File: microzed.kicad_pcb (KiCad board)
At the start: 10 copper layers, 60 x 100 mm, 333 parts, among them IC1 XC7Z020-1CLG484C, IC2 RTL8211E-VL-CG, J1 640456-3, J2 10104111-0001LF, J3 L829-1J1T-43, J4 Micro_SD_Card_Det_Hirose_DM3AT, J5 10104111-0001LF, J6 BSH-090-01-X-D-A, J7 BSH-090-01-X-D-A, Q1 MMBT3904, Q2 MMBT3904, SW1 SW_Push, U1 TLV62130RGTR, U10 MT41K256M16TW, U11 MT25QL128ABA8E12-1SIT, U12 USB3320C-EZK, U13 ASDMB-24.000MHZ-LC-T, U14 ASDMB-25.000MHZ-LC-T, U15 TXS02612RTWR, U16 CP2104-F03-GM, U2 TLV62130RGTR, U3 TLV62130RGTR, U4 TLV62130RGTR, U5 TLV62130RGTR, U6 ASDMB-33.333MHZ-LC-T, U7 TPS51206DSQR, U8 REF3012, U9 MT41K256M16TW

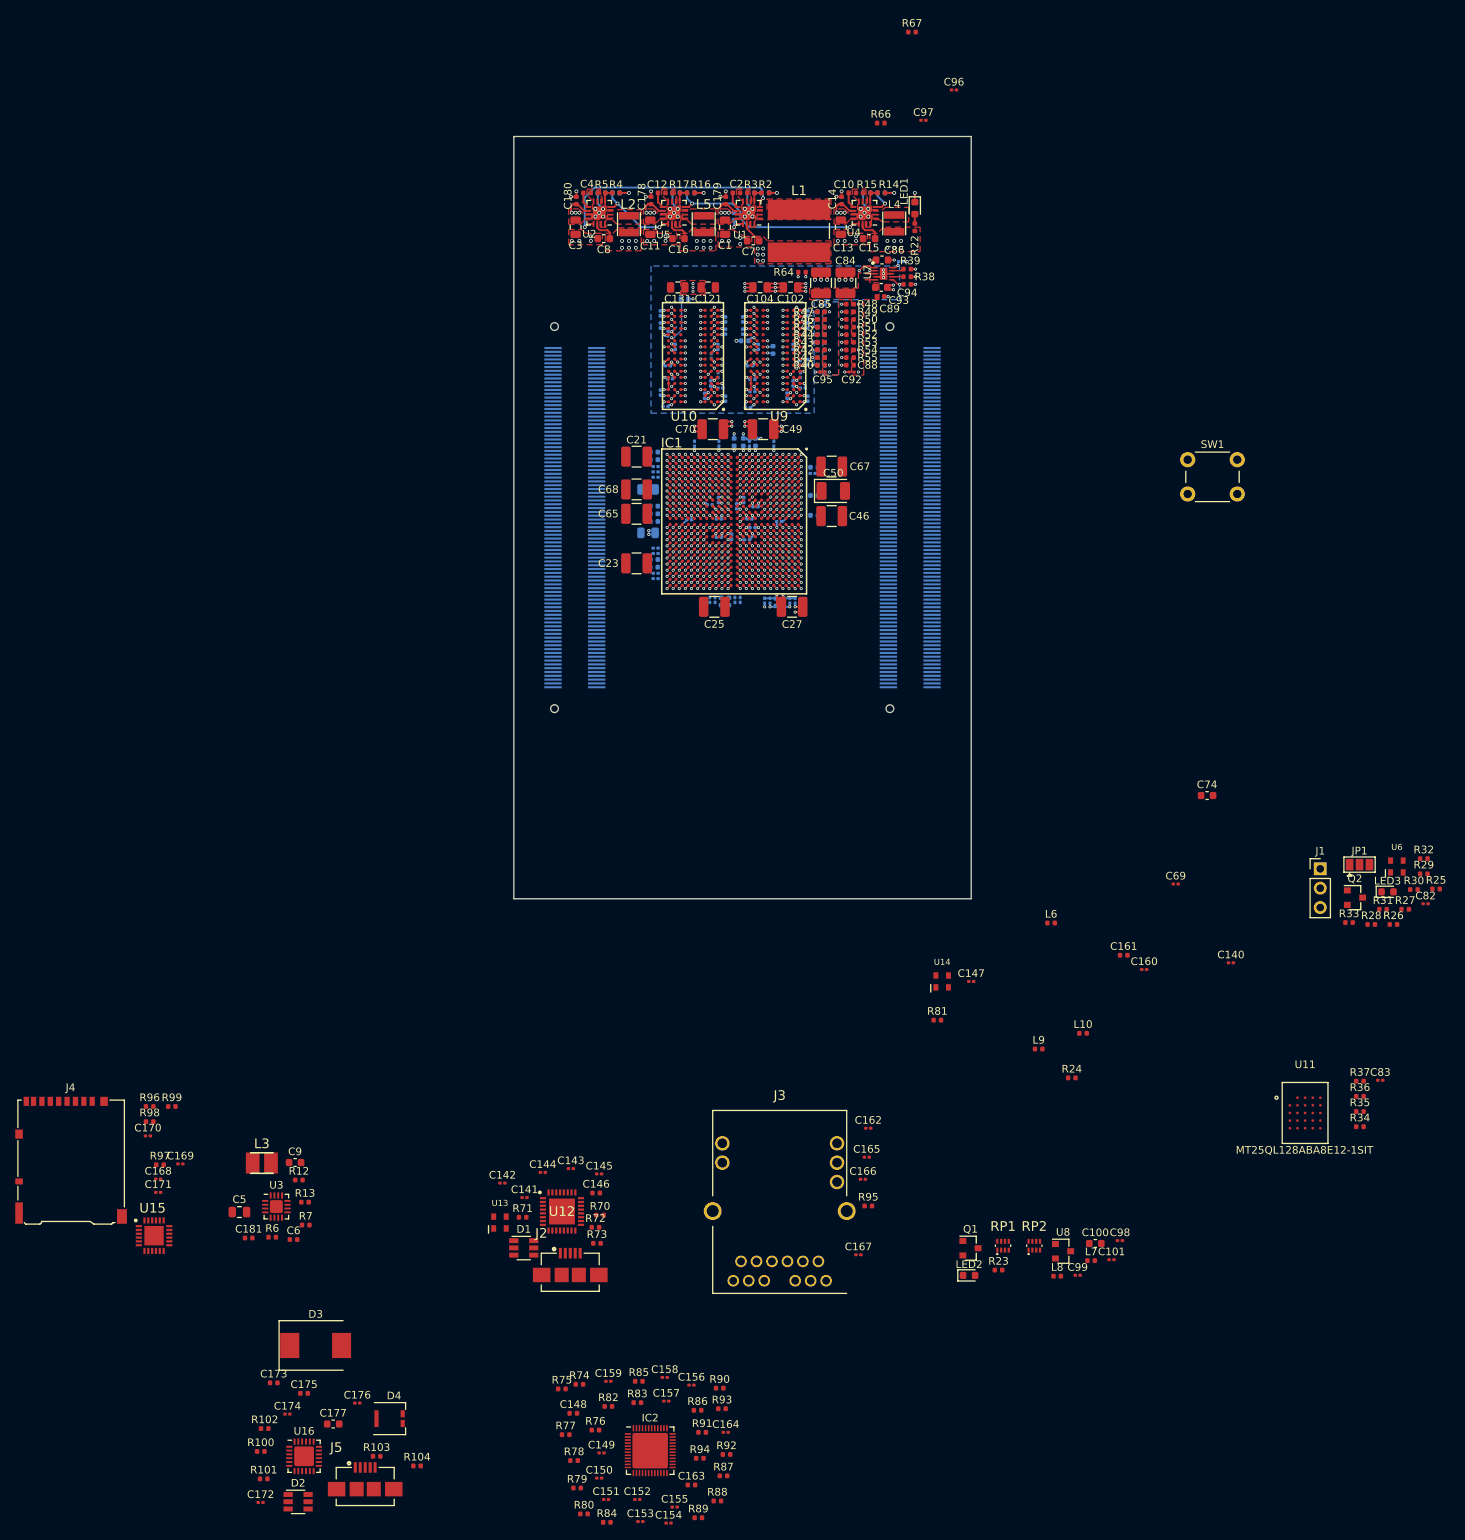
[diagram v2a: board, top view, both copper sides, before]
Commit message: start ethernet related elements
Signed-off-by: Yi Qingliang <niqingliang2003@gmail.com>
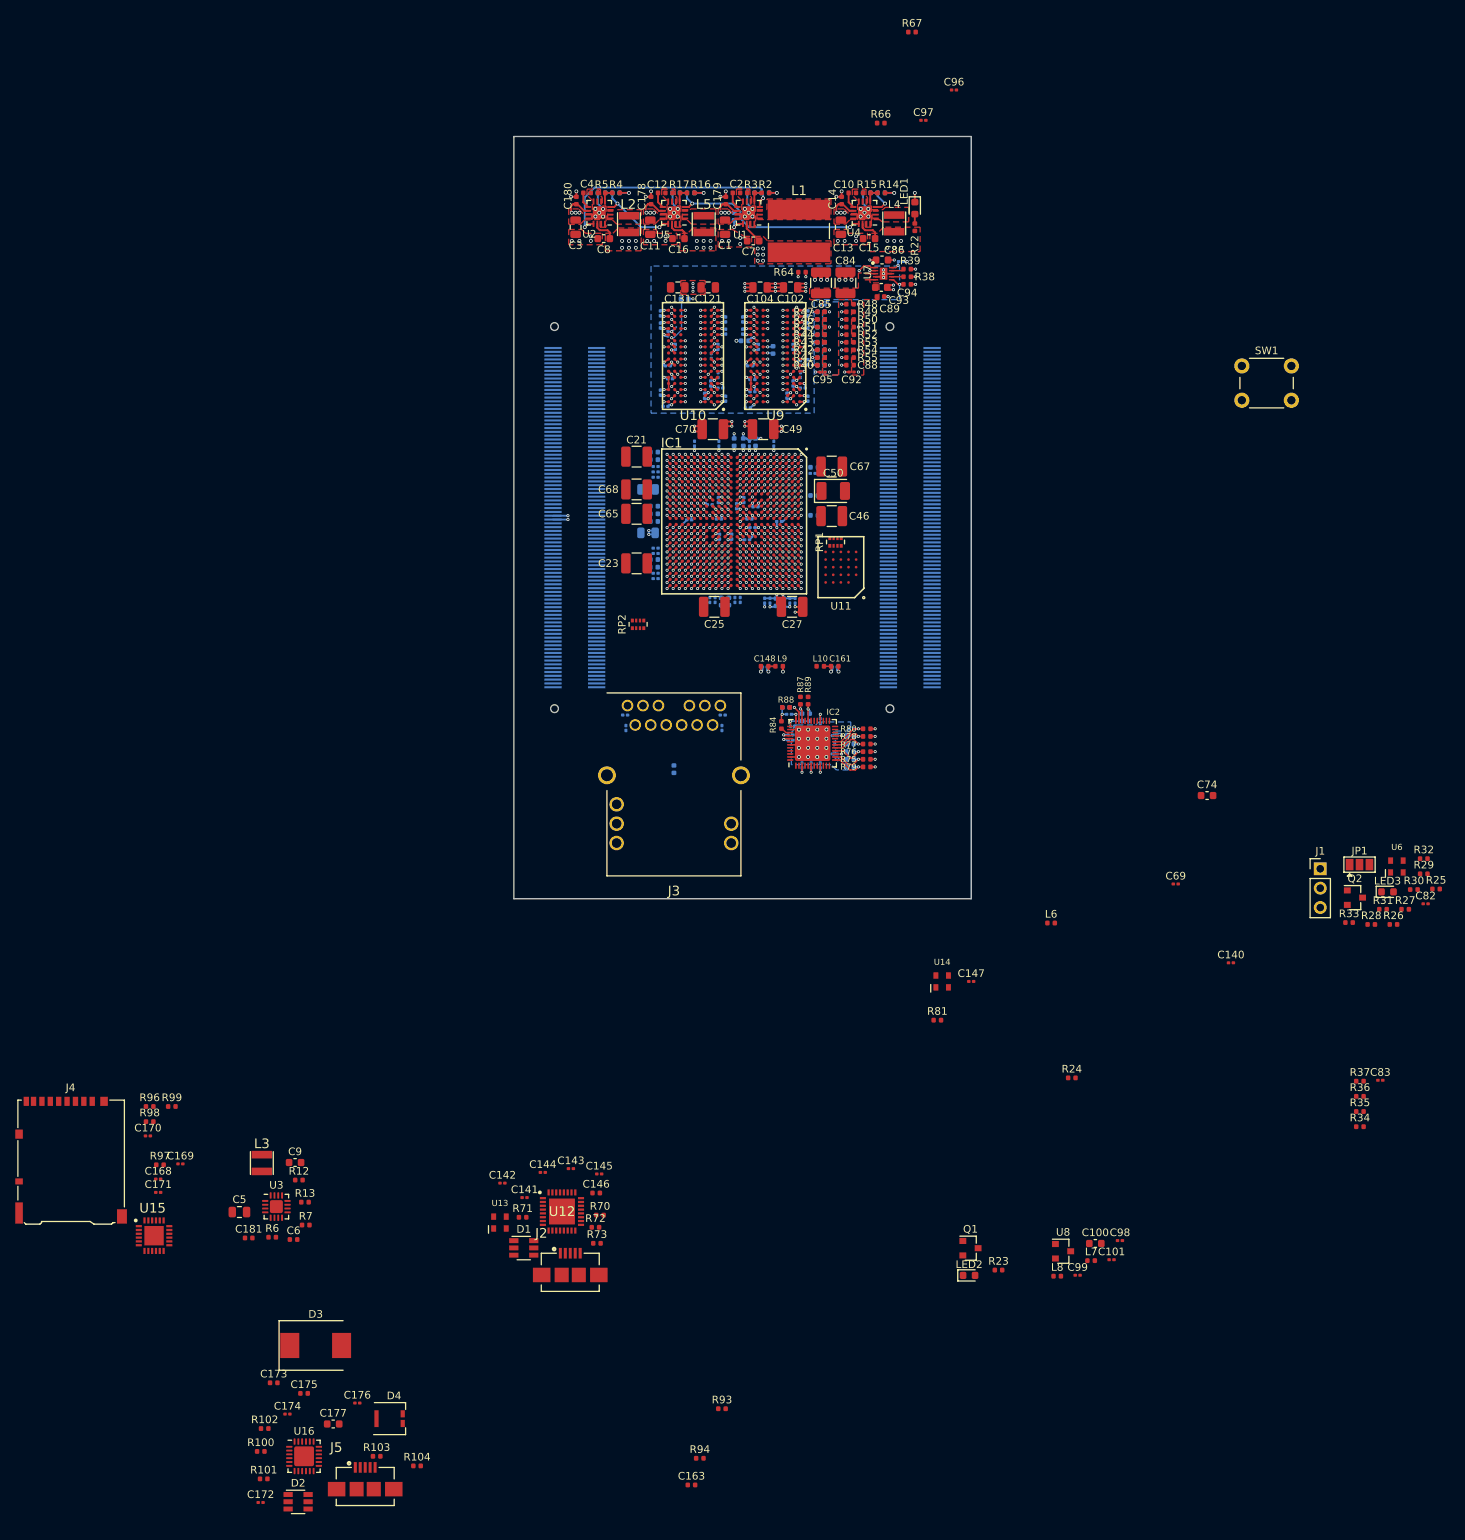
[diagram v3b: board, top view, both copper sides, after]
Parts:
- C149, C150, C151, C152, C153, C154, C155, C156, C157, C158, C159, C160, C162, C164, C165, C166, C167, R74, R82, R83, R85, R86, R90, R91, R92, R95: moved to B.Cu
- RP1, RP2: footprint microzed:YC124FR0749R9L -> Resistor_SMD:R_Array_Convex_4x0402
- U11: footprint microzed:BGA24C100P5X5_600X800X155 -> microzed:BGA-24_6.0x8.0mm_Layout5x5_P1.0mm
- moved R80 109.5 mm to (16.3, 77.7), turned to 180 degrees
- moved R89 108.2 mm to (8.60, 74.0), turned to 270 degrees
- moved R84 107.1 mm to (5.10, 77.2), turned to 90 degrees
- moved C154 105.6 mm to (12.1, 78.6), turned to 180 degrees
- moved C149 105.3 mm to (2.92, 69.6), turned to 180 degrees
- moved C155 104.9 mm to (10.2, 76.7), turned to 270 degrees
- moved R88 104.5 mm to (5.70, 74.9)
- moved C153 103.9 mm to (12.1, 81.0), turned to 180 degrees
- moved C152 103.4 mm to (6.62, 77.4)
- moved R78 102.5 mm to (16.3, 78.7), turned to 180 degrees
- moved R87 102.2 mm to (7.60, 74.0), turned to 270 degrees
- moved R79 101.9 mm to (16.3, 82.7), turned to 180 degrees
- moved C148 101.2 mm to (2.90, 69.5), turned to 180 degrees
- moved C150 100.0 mm to (6.30, 79.2)
- moved C151 100.0 mm to (9.00, 82.5), turned to 90 degrees
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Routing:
- net GND: track 132.4 -> 141.3 mm, vias 176 -> 196
- net Net-(C157-Pad1): track 0.00 -> 6.19 mm, vias 0 -> 4
- net Net-(C148-Pad1): track 0.00 -> 5.02 mm, vias 0 -> 3
- net /ethernet/RXC: track 0.00 -> 4.96 mm, vias 0 -> 1
- net /ethernet/PHY_AD2: track 0.00 -> 4.96 mm, vias 0 -> 1
- net /ethernet/AN0: track 0.00 -> 4.86 mm, vias 0 -> 1
- net /ethernet/TXDLY: track 0.00 -> 4.86 mm, vias 0 -> 1
- net /ethernet/SELRGV: track 0.00 -> 4.86 mm, vias 0 -> 1
- net /ethernet/AN1: track 0.00 -> 4.86 mm, vias 0 -> 1
- net V3V3: track 22.4 -> 27.0 mm, vias 20 -> 22
- net /ethernet/PHY_AD0: track 0.00 -> 2.84 mm, vias 0 -> 1
- net /ethernet/RXDLY: track 0.00 -> 2.76 mm, vias 0 -> 1
- net VCCBRAM: track 30.3 -> 32.4 mm, vias 22 -> 24
- net /ethernet/PHY_AD1: track 0.00 -> 2.01 mm, vias 0 -> 1
- net BANK13_LVDS_6_N: track 0.57 -> 2.53 mm, vias 1 -> 2
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- added copper zone on B.Cu, net GND
- added copper zone on B.Cu, net PWR_B501

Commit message: pcb: ethernet init done
Signed-off-by: Yi Qingliang <niqingliang2003@gmail.com>
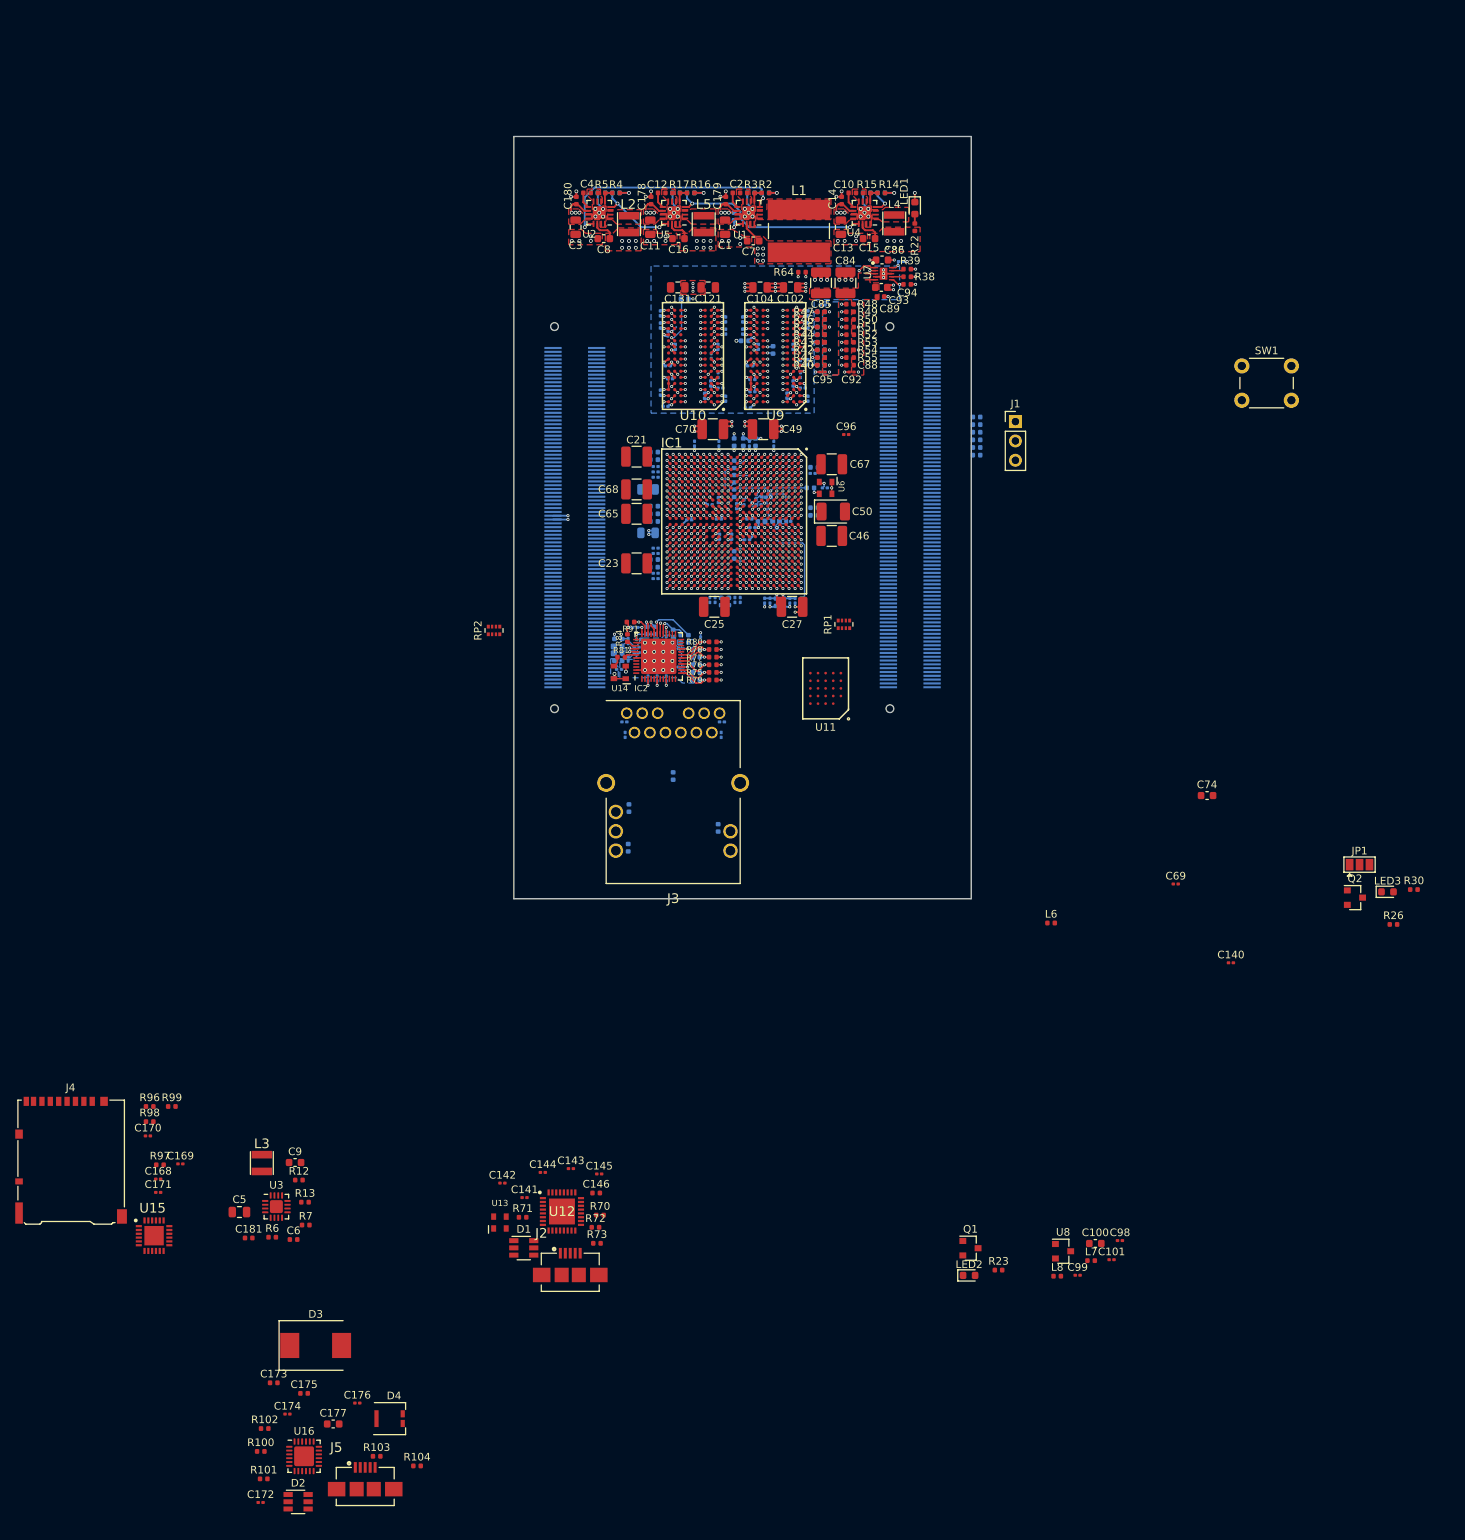
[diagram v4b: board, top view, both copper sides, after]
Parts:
- C147, C148, C161, C163, C82, C83, C97, L10, L9, R24, R25, R27, R28, R29, R31, R32, R33, R34, R35, R36, R37, R66, R67, R87, R88, R89, R93, R94: moved to B.Cu
- R91: moved to F.Cu
- moved R37 112.6 mm to (-1.10, 46.8), turned to 90 degrees
- moved C163 111.7 mm to (-9.10, 65.2), turned to 270 degrees
- moved C83 111.3 mm to (2.80, 47.3), turned to 180 degrees
- moved R35 108.9 mm to (4.40, 50.5), turned to 180 degrees
- moved R36 108.9 mm to (2.50, 50.5), turned to 180 degrees
- moved R94 107.5 mm to (-8.10, 65.9), turned to 270 degrees
- moved R93 101.1 mm to (-7.10, 65.9), turned to 270 degrees
- moved R34 100.5 mm to (7.80, 61.1), turned to 90 degrees
- moved R25 97.5 mm to (8.90, 46.1), turned to 180 degrees
- moved C82 95.9 mm to (10.8, 46.1), turned to 180 degrees
- moved U6 89.9 mm to (10.9, 46.1), turned to 180 degrees
- moved R33 82.4 mm to (30.7, 36.8)
- moved R31 82.2 mm to (30.7, 38.8)
- moved R27 81.9 mm to (30.7, 41.8), turned to 180 degrees
- moved R32 81.8 mm to (30.7, 37.8)
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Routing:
- net Net-(IC1-PadE14): track 0.57 -> 11.7 mm
- net CARRIER_SRST#: track 0.57 -> 9.17 mm
- net ETH_MDIO: track 0.57 -> 7.33 mm, vias 1 -> 2
- net Net-(IC1-PadF7): track 0.57 -> 5.43 mm
- net ETH_RST#: track 0.57 -> 5.04 mm, vias 1 -> 2
- net Net-(IC1-PadN7): track 0.57 -> 4.69 mm
- net Net-(C148-Pad1): track 5.02 -> 2.06 mm, vias 3 -> 2
- net V3V3: track 27.0 -> 29.8 mm, vias 22 -> 23
- net Net-(C157-Pad1): track 6.19 -> 3.40 mm, vias 4 -> 3
- net GND: track 141.3 -> 144.0 mm, vias 196 -> 198
- net VCCO_DDR: track 61.5 -> 64.0 mm
- net VCCO_34: track 3.39 -> 5.29 mm
- net BANK34_LVDS_3_P: track 0.57 -> 2.46 mm
- net Net-(IC2-Pad42): track 0.00 -> 1.61 mm
- net Net-(IC1-PadM7): track 0.57 -> 2.07 mm
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- added copper zone on B.Cu, net Net-(C148-Pad1)
- added copper zone on In4.Cu.VDD, net Net-(C148-Pad1)
- added copper zone on B.Cu, net Net-(C157-Pad1)
- added copper zone on In5.Cu.GND, net Net-(C157-Pad1)
- added copper zone on B.Cu, net Net-(C83-Pad1)
- added copper zone on B.Cu, net V3V3

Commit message: pcb: vttref capacitor done
Signed-off-by: Yi Qingliang <niqingliang2003@gmail.com>
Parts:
- C96: moved to B.Cu
- moved C96 18.1 mm to (-2.70, 47.0)
- moved C64 1.10 mm to (-3.30, 48.8)
- moved C80 0.50 mm to (-4.30, 47.8)
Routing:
- net GND: track 144.0 -> 145.0 mm
- net VTTREF: track 7.68 -> 8.38 mm
